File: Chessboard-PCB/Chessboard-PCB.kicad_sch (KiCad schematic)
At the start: 37 parts, among them IC1 SS49E, IC10 SS49E, IC11 SS49E, IC12 SS49E, IC13 SS49E, IC14 SS49E, IC15 SS49E, IC16 SS49E, IC17 SS49E, IC18 SS49E, IC19 SS49E, IC2 SS49E, IC20 SS49E, IC21 SS49E, IC22 SS49E, IC23 SS49E, IC24 SS49E, IC25 SS49E, IC26 SS49E, IC27 SS49E, IC28 SS49E, IC29 SS49E, IC3 SS49E, IC30 SS49E, IC31 SS49E, IC32 SS49E, IC4 SS49E, IC5 SS49E, IC6 SS49E, IC7 SS49E, IC8 SS49E, IC9 SS49E, J1 Conn_01x08, J2 Conn_01x02, J3 Conn_01x08, J4 Conn_01x08, J5 Conn_01x08

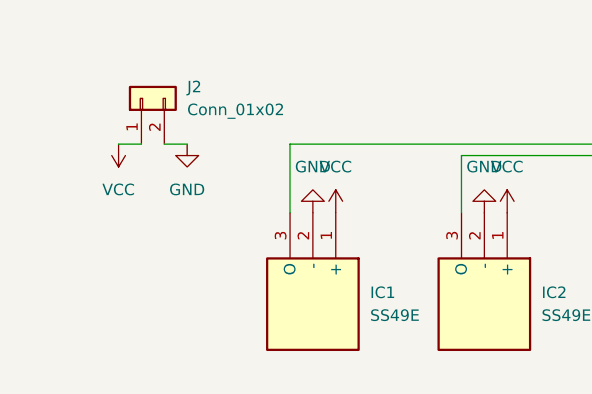
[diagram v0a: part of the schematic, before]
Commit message: Delete unneeded Kicad stuff
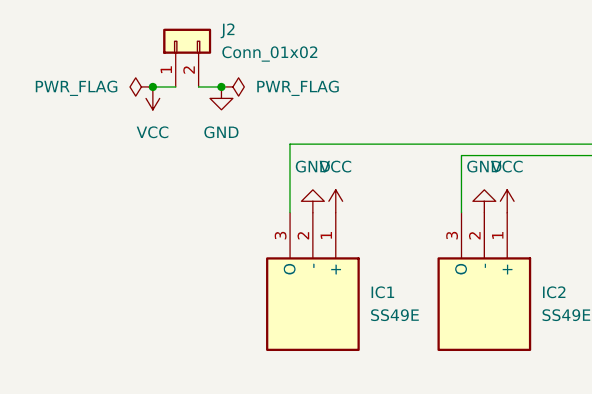
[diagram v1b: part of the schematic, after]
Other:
- moved on the sheet: J2
